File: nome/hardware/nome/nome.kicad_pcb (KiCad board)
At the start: 2 copper layers, 91.4 x 91.4 mm, 59 parts, among them J1 SJ-2524, J2 JTAG_SWD, J3 JST, J4 7SEG_DEBUG, SW1 SW_SPDT, SW2 Rotary_Encoder_Switch, U1 LM1117-1.8, U2 LM1117-3.3, U3 AS1115, U4 STMF411CEU6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

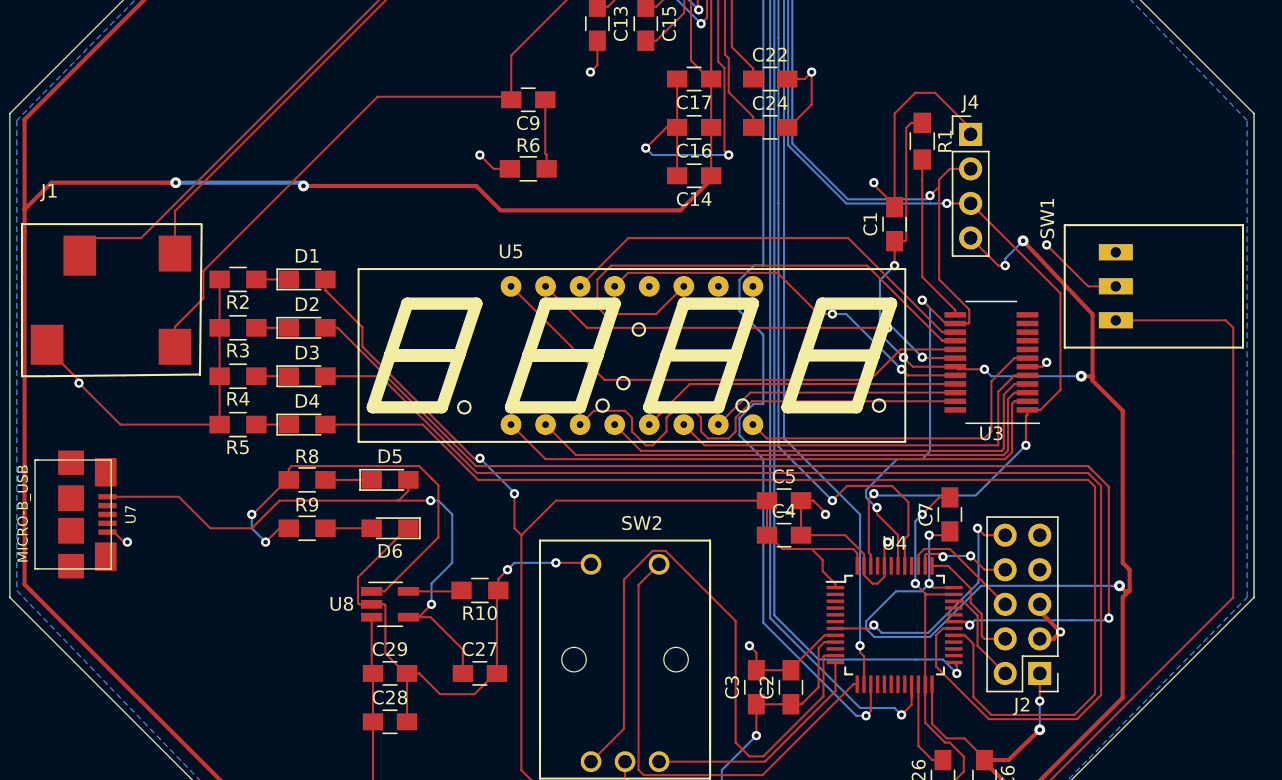
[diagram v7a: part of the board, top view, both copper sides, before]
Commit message: Add mounting holes
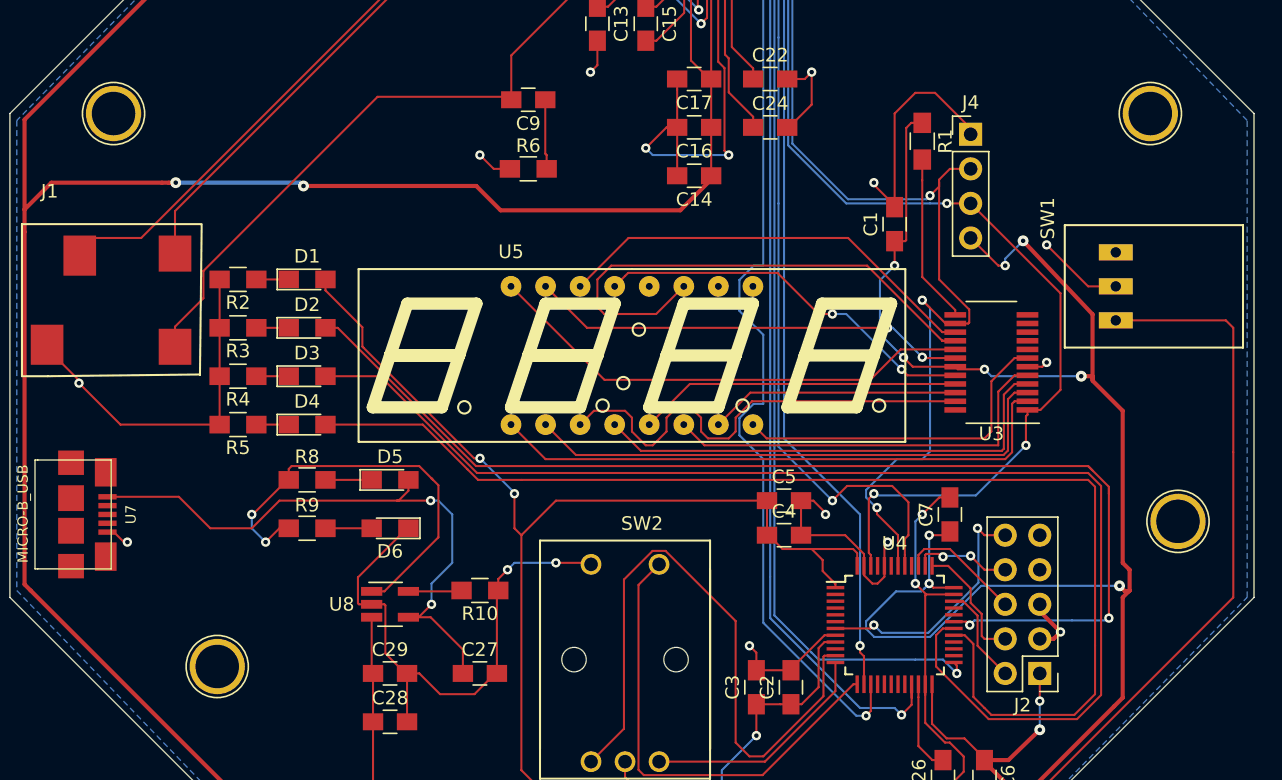
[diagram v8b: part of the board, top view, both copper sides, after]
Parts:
- added ?: Mount, Connectors:1pin, F.Cu at (106.2, 96.0)
- added ?: Mount, Connectors:1pin, F.Cu at (35.6, 106.7)
- added ?: Mount, Connectors:1pin, F.Cu at (104.1, 66.0)
- added ?: Mount, Connectors:1pin, F.Cu at (27.9, 66.0)
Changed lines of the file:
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@@
   (tracks 937)
   (zones 0)
-  (modules 59)
+  (modules 63)
   (nets 107)
 )
@@
   (mod_text_size 1 1)
   (mod_text_width 0.15)
-  (pad_size 1.5 1.5)
-  (pad_drill 0.6)
+  (pad_size 4.064 4.064)
+  (pad_drill 3.2)
   (pad_to_mask_clearance 0)
   (aux_axis_origin 0 0)
@@
   (add_net +3V3)
 )
+  (module Connectors:1pin (layer F.Cu)
+    (at 106.172 96.012)
+    (descr "module 1 pin (ou trou mecanique de percage)")
+    (tags DEV)
+    (fp_text reference "" (at 0 -3.048) (layer F.SilkS)
+      (effects (font (size 1 1) (thickness 0.15)))
+    )
+    (fp_text value Mount (at 0 3) (layer F.Fab)
+      (effects (font (size 1 1) (thickness 0.15)))
+    )
+    (fp_circle (center 0 0) (end 2 0.8) (layer F.Fab) (width 0.1))
+    (fp_circle (center 0 0) (end 2.6 0) (layer F.CrtYd) (width 0.05))
+    (fp_circle (center 0 0) (end 0 -2.286) (layer F.SilkS) (width 0.12))
+    (pad "" np_thru_hole circle (at 0 0) (size 4.064 4.064) (drill 3.2) (layers *.Cu *.Mask))
+  )
+  (module Connectors:1pin (layer F.Cu)
+    (at 35.56 106.68)
+    (descr "module 1 pin (ou trou mecanique de percage)")
+    (tags DEV)
+    (fp_text reference "" (at 0 -3.048) (layer F.SilkS)
+      (effects (font (size 1 1) (thickness 0.15)))
+    )
+    (fp_text value Mount (at 0 3) (layer F.Fab)
+      (effects (font (size 1 1) (thickness 0.15)))
+    )
+    (fp_circle (center 0 0) (end 2 0.8) (layer F.Fab) (width 0.1))
+    (fp_circle (center 0 0) (end 2.6 0) (layer F.CrtYd) (width 0.05))
+    (fp_circle (center 0 0) (end 0 -2.286) (layer F.SilkS) (width 0.12))
+    (pad "" np_thru_hole circle (at 0 0) (size 4.064 4.064) (drill 3.2) (layers *.Cu *.Mask))
+  )
+  (module Connectors:1pin (layer F.Cu)
+    (at 104.14 66.04)
+    (descr "module 1 pin (ou trou mecanique de percage)")
+    (tags DEV)
+    (fp_text reference "" (at 0 -3.048) (layer F.SilkS)
+      (effects (font (size 1 1) (thickness 0.15)))
+    )
+    (fp_text value Mount (at 0 3) (layer F.Fab)
+      (effects (font (size 1 1) (thickness 0.15)))
+    )
+    (fp_circle (center 0 0) (end 2 0.8) (layer F.Fab) (width 0.1))
+    (fp_circle (center 0 0) (end 2.6 0) (layer F.CrtYd) (width 0.05))
+    (fp_circle (center 0 0) (end 0 -2.286) (layer F.SilkS) (width 0.12))
+    (pad "" np_thru_hole circle (at 0 0) (size 4.064 4.064) (drill 3.2) (layers *.Cu *.Mask))
+  )
+  (module Connectors:1pin (layer F.Cu)
+    (at 27.94 66.04)
+    (descr "module 1 pin (ou trou mecanique de percage)")
+    (tags DEV)
+    (fp_text reference "" (at 0 -3.048) (layer F.SilkS)
+      (effects (font (size 1 1) (thickness 0.15)))
+    )
+    (fp_text value Mount (at 0 3) (layer F.Fab)
+      (effects (font (size 1 1) (thickness 0.15)))
+    )
+    (fp_circle (center 0 0) (end 2 0.8) (layer F.Fab) (width 0.1))
+    (fp_circle (center 0 0) (end 2.6 0) (layer F.CrtYd) (width 0.05))
+    (fp_circle (center 0 0) (end 0 -2.286) (layer F.SilkS) (width 0.12))
+    (pad "" np_thru_hole circle (at 0 0) (size 4.064 4.064) (drill 3.2) (layers *.Cu *.Mask))
+  )
   (module Housings_QFP:LQFP-48_7x7mm_Pitch0.5mm (layer F.Cu)
     (at 85.344 103.632)
